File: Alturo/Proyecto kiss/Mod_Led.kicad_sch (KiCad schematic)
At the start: 33 parts, among them U5 ULN2003

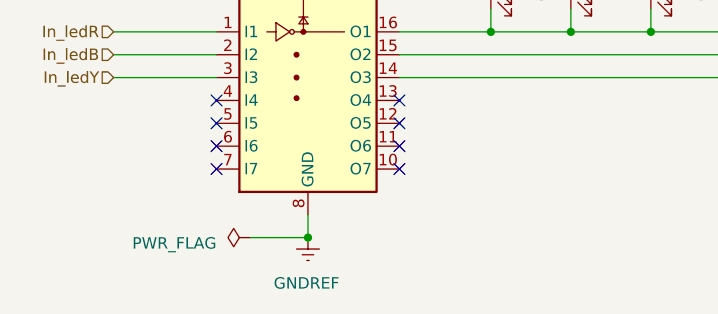
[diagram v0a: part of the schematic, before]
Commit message: Update Mod_Led.kicad_sch
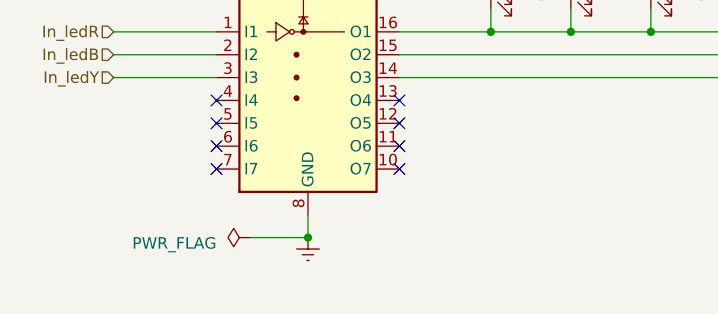
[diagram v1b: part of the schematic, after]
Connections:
- net GNDREF renamed Earth
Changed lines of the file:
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@@
   (junction (at 234.95 60.96) (diameter 0) (color 0 0 0 0)
   )
+  (junction (at 82.55 109.22) (diameter 0) (color 0 0 0 0)
+  )
   (junction (at 185.42 60.96) (diameter 0) (color 0 0 0 0)
   )
@@
   )
   (junction (at 226.06 60.96) (diameter 0) (color 0 0 0 0)
-  )
-  (junction (at 82.55 109.22) (diameter 0) (color 0 0 0 0)
   )
   (junction (at 111.76 86.36) (diameter 0) (color 0 0 0 0)
@@
     )
   )
-  (symbol (lib_id "power:GNDREF") (at 82.55 109.22 0) (unit 1)
-    (in_bom yes) (on_board yes) (dnp no)
-    (property "Reference" "#PWR09" (at 82.55 115.57 0)
-      (effects (font (size 1.27 1.27)) hide)
-    )
-    (property "Value" "GNDREF" (at 78.74 114.3 0)
-      (effects (font (size 1.27 1.27)) (justify left))
-    )
-    (property "Footprint" "" (at 82.55 109.22 0)
-      (effects (font (size 1.27 1.27)) hide)
-    )
-    (property "Datasheet" "" (at 82.55 109.22 0)
-      (effects (font (size 1.27 1.27)) hide)
-    )
-    (pin "1")
-    (instances
-      (project "KISS_V2"
-        (path "/65dfba5e-78e0-455d-92b3-d370168d98c5/769603bd-ecbf-46b5-a166-ba7906ee1166"
-          (reference "#PWR09") (unit 1)
-        )
-      )
-      (project "driver"
-        (path "/e72c8f76-7b49-4479-9cd2-c8df4a0571e7"
-          (reference "#PWR?") (unit 1)
-        )
-      )
-      (project "Proyecto kiss"
-        (path "/e9fd9658-b200-4aa5-b329-c1636df53c02/43ce7ec9-de9c-4a2d-b356-863f187df326"
-          (reference "#PWR01") (unit 1)
-        )
-      )
-    )
-  )
   (symbol (lib_id "Device:R") (at 185.42 68.58 0) (unit 1)
     (in_bom yes) (on_board yes) (dnp no) (fields_autoplaced)
@@
         )
       )
+    )
+  )
+  (symbol (lib_id "power:Earth") (at 82.55 109.22 0) (unit 1)
+    (in_bom yes) (on_board yes) (dnp no) (fields_autoplaced)
+    (property "Reference" "#PWR04" (at 82.55 115.57 0)
+      (effects (font (size 1.27 1.27)) hide)
+    )
+    (property "Value" "Earth" (at 82.55 113.03 0)
+      (effects (font (size 1.27 1.27)) hide)
+    )
+    (property "Footprint" "" (at 82.55 109.22 0)
+      (effects (font (size 1.27 1.27)) hide)
+    )
+    (property "Datasheet" "~" (at 82.55 109.22 0)
+      (effects (font (size 1.27 1.27)) hide)
+    )
+    (pin "1")
+    (instances
+      (project "KISS_V2"
+        (path "/65dfba5e-78e0-455d-92b3-d370168d98c5/4b3fec45-17f7-4493-b982-1ebc81656281"
+          (reference "#PWR04") (unit 1)
+        )
+      )
+      (project "Proyecto kiss"
+        (path "/e9fd9658-b200-4aa5-b329-c1636df53c02"
+          (reference "#PWR02") (unit 1)
+        )
+        (path "/e9fd9658-b200-4aa5-b329-c1636df53c02/43ce7ec9-de9c-4a2d-b356-863f187df326"
+          (reference "#PWR01") (unit 1)
+        )
+      )
